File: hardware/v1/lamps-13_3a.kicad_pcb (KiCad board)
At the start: 2 copper layers, 226.7 x 19.7 mm, 19 parts, among them P1 CONN_02X05, P2 CONN_01X04, P3 CONN_01X04

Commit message: Replace LED footprints in lamps-13_3a, and delete additional unneded gerber outputs.
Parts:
- D1, D10, D11, D12, D13, D14, D15, D16, D2, D3, D4, D5, D6, D7, D8, D9: footprint LEDs:LED-5MM -> myparts:LED-5MM-custom

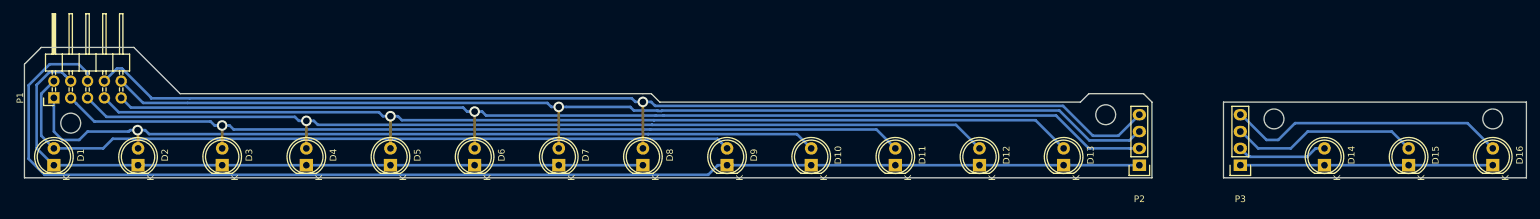
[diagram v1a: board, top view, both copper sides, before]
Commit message: Add new M3 drill mark pads to lamsp-13-3a
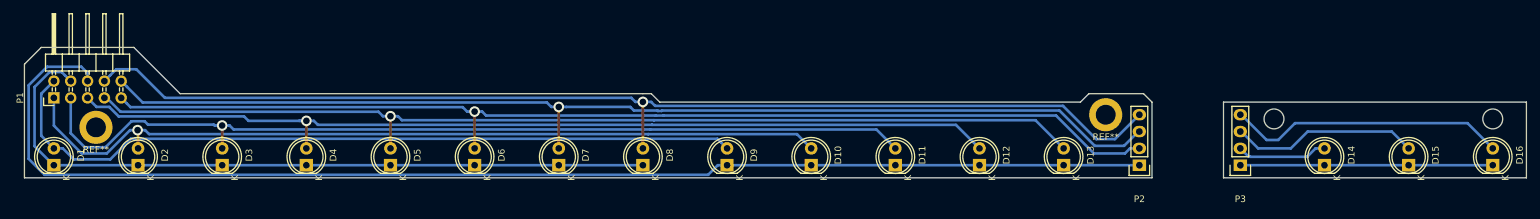
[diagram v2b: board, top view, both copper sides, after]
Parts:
- added REF**: M3, myparts:HOLE_M3, F.Cu at (209.6, 106.7)
- added REF**: M3, myparts:HOLE_M3, F.Cu at (57.1, 108.6)
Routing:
- net /SEG2: track 131.1 -> 137.4 mm
- net /SEG0: track 114.5 -> 115.9 mm
- net /SEG1: track 124.4 -> 125.6 mm
- net /SEG6: track 164.2 -> 164.9 mm
- net /SEG5: track 162.4 -> 163.0 mm
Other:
- outline, holes or cut-outs redrawn

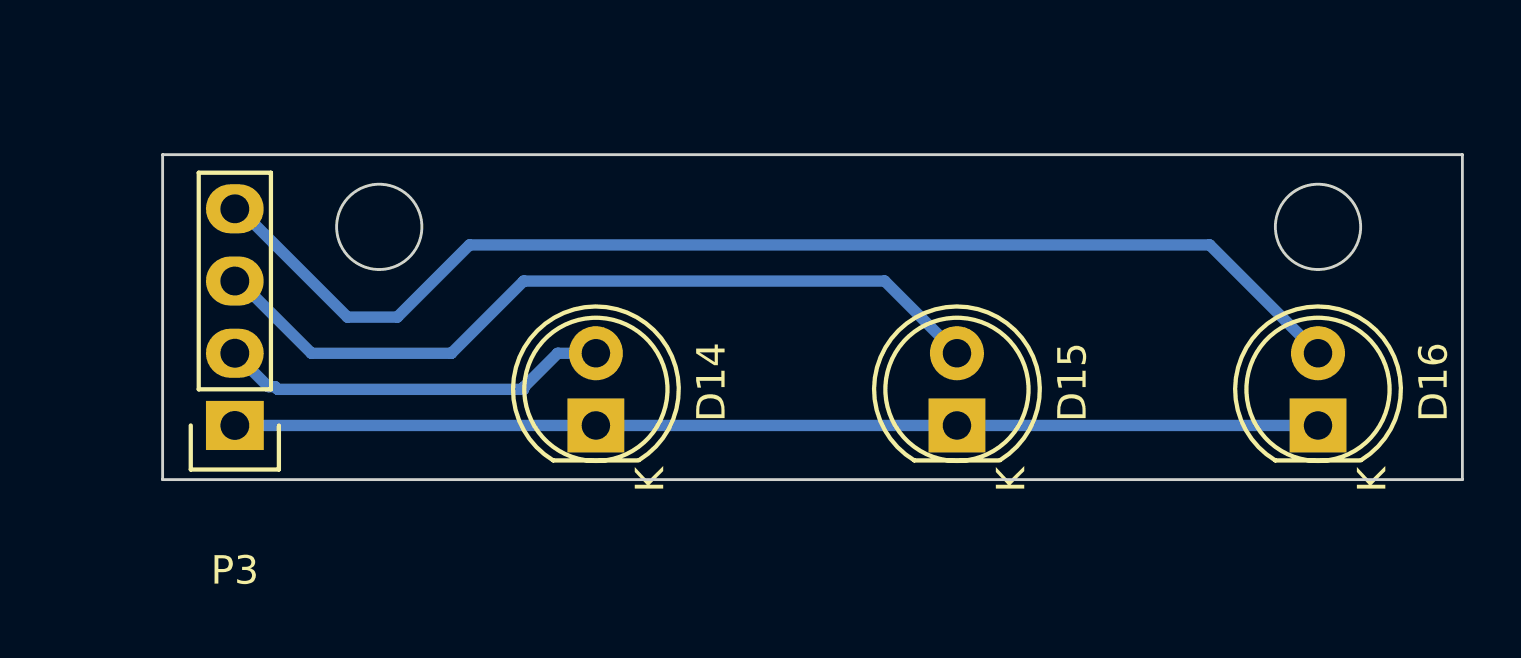
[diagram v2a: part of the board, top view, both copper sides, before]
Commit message: Add m3 holes and re-route around them for led boards.
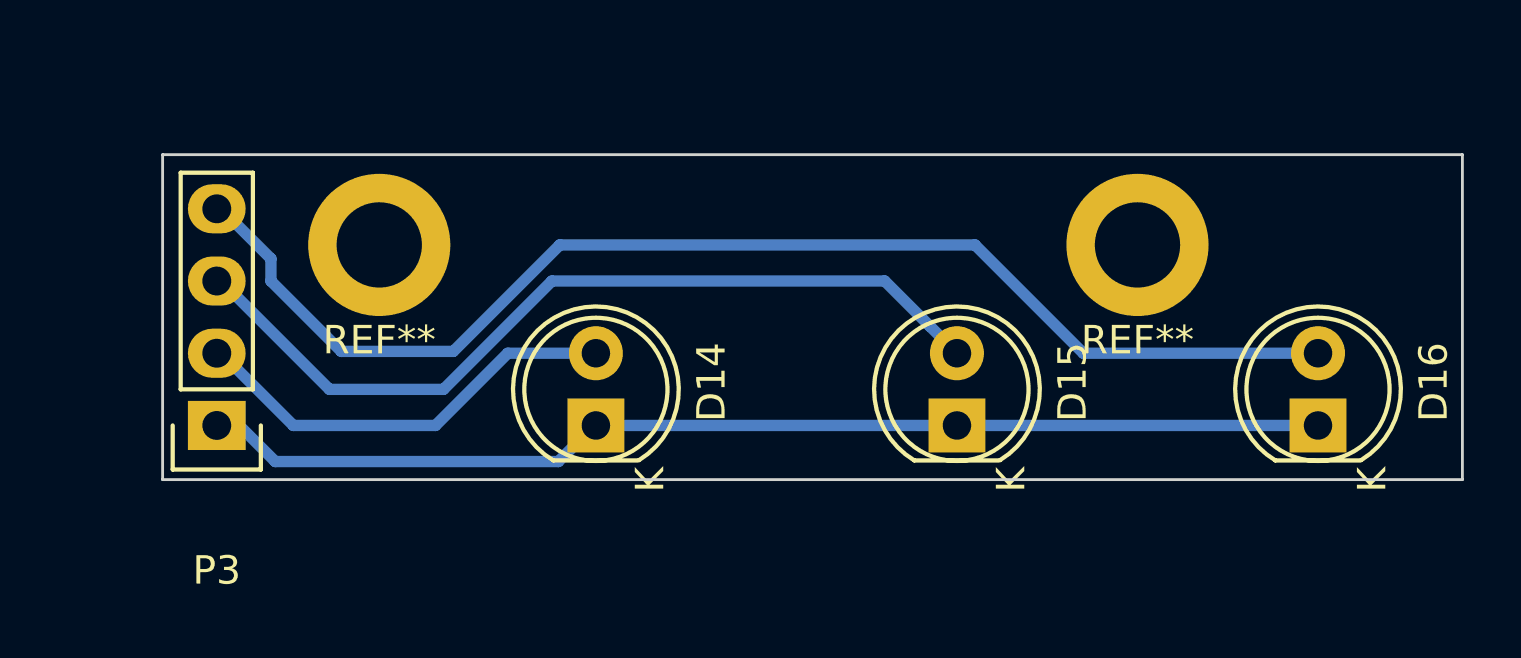
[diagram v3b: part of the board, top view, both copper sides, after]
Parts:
- added REF**: M3, myparts:HOLE_M3, F.Cu at (261.6, 108.0)
- added REF**: M3, myparts:HOLE_M3, F.Cu at (234.9, 108.0)
- moved P3 0.63 mm to (229.2, 114.3)
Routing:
- net Net-(D16-Pad2): track 42.3 -> 44.6 mm
- net Net-(D15-Pad2): track 28.6 -> 30.2 mm
- net Net-(D14-Pad2): track 13.8 -> 15.4 mm
- net Net-(D14-Pad1): track 38.3 -> 39.0 mm
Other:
- outline, holes or cut-outs redrawn
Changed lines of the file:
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@@
     (area 34.545001 90.614999 284.225 124.620001)
     (thickness 1.6)
-    (drawings 25)
-    (tracks 182)
+    (drawings 23)
+    (tracks 187)
     (zones 0)
-    (modules 21)
+    (modules 23)
     (nets 15)
   )
@@
   )
   (module Pin_Headers:Pin_Header_Straight_1x04 (layer F.Cu)
-    (at 229.87 114.3 180)
+    (at 229.235 114.3 180)
     (descr "Through hole pin header")
     (tags "pin header")
@@
     (pad 1 thru_hole circle (at 0 0) (size 5 5) (drill 3) (layers *.Cu *.Mask F.SilkS))
   )
+  (module myparts:HOLE_M3 (layer F.Cu)
+    (at 261.62 107.95)
+    (fp_text reference REF** (at 0 3.35) (layer F.SilkS)
+      (effects (font (size 1 1) (thickness 0.15)))
+    )
+    (fp_text value M3 (at 0 -3.5) (layer F.Fab)
+      (effects (font (size 1 1) (thickness 0.15)))
+    )
+    (fp_circle (center 0 0) (end 1.5 0) (layer B.Fab) (width 0.15))
+    (pad 1 thru_hole circle (at 0 0) (size 5 5) (drill 3) (layers *.Cu *.Mask F.SilkS))
+  )
+  (module myparts:HOLE_M3 (layer F.Cu)
+    (at 234.95 107.95)
+    (fp_text reference REF** (at 0 3.35) (layer F.SilkS)
+      (effects (font (size 1 1) (thickness 0.15)))
+    )
+    (fp_text value M3 (at 0 -3.5) (layer F.Fab)
+      (effects (font (size 1 1) (thickness 0.15)))
+    )
+    (fp_circle (center 0 0) (end 1.5 0) (layer B.Fab) (width 0.15))
+    (pad 1 thru_hole circle (at 0 0) (size 5 5) (drill 3) (layers *.Cu *.Mask F.SilkS))
+  )
   (dimension 12.7 (width 0.3) (layer F.SilkS)
     (gr_text "12.700 mm" (at 120.65 118.825) (layer F.SilkS)
@@
   (gr_line (start 69.85 103.505) (end 62.865 96.52) (layer Edge.Cuts) (width 0.1))
   (gr_line (start 216.535 116.205) (end 216.535 104.775) (layer Edge.Cuts) (width 0.1))
-  (gr_circle (center 234.95 107.315) (end 236.45 107.315) (layer Edge.Cuts) (width 0.1))
-  (gr_circle (center 267.97 107.315) (end 269.47 107.315) (layer Edge.Cuts) (width 0.1))
   (gr_line (start 227.33 116.205) (end 273.05 116.205) (layer Edge.Cuts) (width 0.1))
   (gr_line (start 227.33 104.775) (end 227.33 116.205) (layer Edge.Cuts) (width 0.1))
@@
   (via (at 139.697171 104.74499) (size 1.6) (drill 1) (layers F.Cu B.Cu) (net 10))
   (segment (start 214.63 106.68) (end 214.4776 106.68) (width 0.4) (layer B.Cu) (net 10) (status 30))
-  (segment (start 242.57 114.3) (end 229.87 114.3) (width 0.4) (layer B.Cu) (net 11) (status 30))
-  (segment (start 230.0224 114.3) (end 229.87 114.3) (width 0.4) (layer B.Cu) (net 11) (status 30))
+  (segment (start 230.0224 114.3) (end 231.2924 115.57) (width 0.4) (layer B.Cu) (net 11))
+  (segment (start 231.2924 115.57) (end 241.25 115.57) (width 0.4) (layer B.Cu) (net 11))
+  (segment (start 241.25 115.57) (end 242.52 114.3) (width 0.4) (layer B.Cu) (net 11))
+  (segment (start 242.52 114.3) (end 242.57 114.3) (width 0.4) (layer B.Cu) (net 11))
   (segment (start 255.27 114.3) (end 267.97 114.3) (width 0.4) (layer B.Cu) (net 11) (status 30))
   (segment (start 242.57 114.3) (end 255.27 114.3) (width 0.4) (layer B.Cu) (net 11) (status 30))
-  (segment (start 229.87 111.76) (end 231.046399 112.936399) (width 0.4) (layer B.Cu) (net 12) (status 10))
-  (segment (start 231.379602 113.03) (end 240.03 113.03) (width 0.4) (layer B.Cu) (net 12))
-  (segment (start 240.03 112.956498) (end 241.226498 111.76) (width 0.4) (layer B.Cu) (net 12))
-  (segment (start 241.226498 111.76) (end 242.57 111.76) (width 0.4) (layer B.Cu) (net 12) (status 20))
-  (segment (start 231.046399 112.936399) (end 231.286001 112.936399) (width 0.4) (layer B.Cu) (net 12))
-  (segment (start 231.286001 112.936399) (end 231.379602 113.03) (width 0.4) (layer B.Cu) (net 12))
-  (segment (start 240.03 113.03) (end 240.03 112.956498) (width 0.4) (layer B.Cu) (net 12))
-  (segment (start 229.87 109.22) (end 230.0224 109.22) (width 0.4) (layer B.Cu) (net 13) (status 30))
-  (segment (start 230.0224 109.22) (end 232.5624 111.76) (width 0.4) (layer B.Cu) (net 13) (status 10))
-  (segment (start 232.5624 111.76) (end 237.49 111.76) (width 0.4) (layer B.Cu) (net 13))
-  (segment (start 237.49 111.76) (end 240.03 109.22) (width 0.4) (layer B.Cu) (net 13))
-  (segment (start 240.03 109.22) (end 252.73 109.22) (width 0.4) (layer B.Cu) (net 13))
-  (segment (start 252.73 109.22) (end 255.27 111.76) (width 0.4) (layer B.Cu) (net 13) (status 20))
+  (segment (start 242.57 111.76) (end 239.469929 111.76) (width 0.4) (layer B.Cu) (net 12))
+  (segment (start 231.9274 114.3) (end 229.3874 111.76) (width 0.4) (layer B.Cu) (net 12))
+  (segment (start 229.3874 111.76) (end 229.235 111.76) (width 0.4) (layer B.Cu) (net 12))
+  (segment (start 239.469929 111.76) (end 236.929929 114.3) (width 0.4) (layer B.Cu) (net 12))
+  (segment (start 236.929929 114.3) (end 231.9274 114.3) (width 0.4) (layer B.Cu) (net 12))
+  (segment (start 233.1974 113.03) (end 237.209964 113.03) (width 0.4) (layer B.Cu) (net 13))
+  (segment (start 241.019964 109.22) (end 252.73 109.22) (width 0.4) (layer B.Cu) (net 13))
+  (segment (start 252.73 109.22) (end 254.320001 110.810001) (width 0.4) (layer B.Cu) (net 13))
+  (segment (start 229.3874 109.22) (end 233.1974 113.03) (width 0.4) (layer B.Cu) (net 13))
+  (segment (start 229.235 109.22) (end 229.3874 109.22) (width 0.4) (layer B.Cu) (net 13))
+  (segment (start 237.209964 113.03) (end 241.019964 109.22) (width 0.4) (layer B.Cu) (net 13))
+  (segment (start 254.320001 110.810001) (end 255.27 111.76) (width 0.4) (layer B.Cu) (net 13))
+  (segment (start 255.905 107.95) (end 259.715 111.76) (width 0.4) (layer B.Cu) (net 14))
+  (segment (start 259.715 111.76) (end 267.97 111.76) (width 0.4) (layer B.Cu) (net 14))
+  (segment (start 241.3 107.95) (end 255.905 107.95) (width 0.4) (layer B.Cu) (net 14))
+  (segment (start 229.235 106.68) (end 229.3874 106.68) (width 0.4) (layer B.Cu) (net 14))
+  (segment (start 229.3874 106.68) (end 231.14 108.4326) (width 0.4) (layer B.Cu) (net 14))
+  (segment (start 231.14 108.4326) (end 231.14 109.22) (width 0.4) (layer B.Cu) (net 14))
+  (segment (start 231.14 109.22) (end 233.614989 111.694989) (width 0.4) (layer B.Cu) (net 14))
+  (segment (start 233.614989 111.694989) (end 237.555011 111.694989) (width 0.4) (layer B.Cu) (net 14))
+  (segment (start 237.555011 111.694989) (end 241.3 107.95) (width 0.4) (layer B.Cu) (net 14))
   (segment (start 229.87 106.68) (end 230.0224 106.68) (width 0.4) (layer B.Cu) (net 14) (status 30))
-  (segment (start 230.0224 106.68) (end 233.8324 110.49) (width 0.4) (layer B.Cu) (net 14) (status 10))
-  (segment (start 233.8324 110.49) (end 235.585 110.49) (width 0.4) (layer B.Cu) (net 14))
-  (segment (start 235.585 110.49) (end 238.125 107.95) (width 0.4) (layer B.Cu) (net 14))
-  (segment (start 238.125 107.95) (end 264.16 107.95) (width 0.4) (layer B.Cu) (net 14))
-  (segment (start 264.16 107.95) (end 267.97 111.76) (width 0.4) (layer B.Cu) (net 14) (status 20))
 )
